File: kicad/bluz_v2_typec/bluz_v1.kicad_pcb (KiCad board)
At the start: 2 copper layers, 29.5 x 17.5 mm, 76 parts, among them J10 Conn, J11 Conn, J12 BTAnt, J2 Conn, J3 Conn, J4 Conn, J5 Conn, J6 Conn, J7 Conn, J8 Conn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

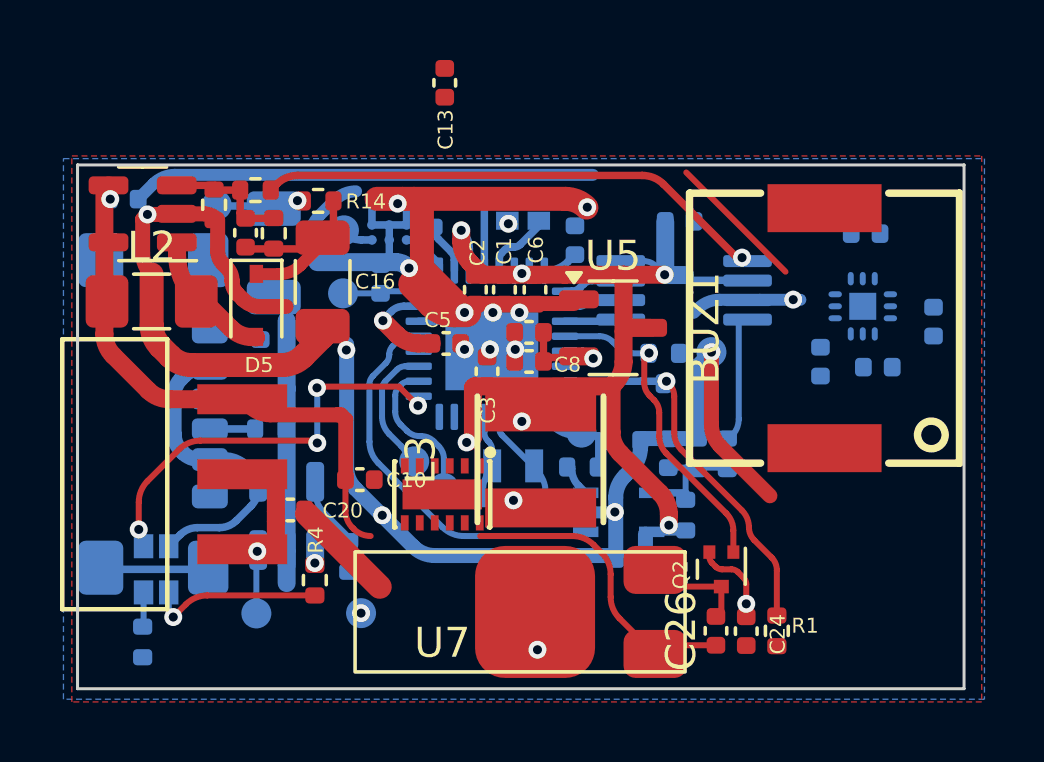
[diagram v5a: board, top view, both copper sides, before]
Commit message: удалено:       kicad/bluz_v2_typec/bluz_v1-backups/bluz_v1-2026-01-23_152519.zip 	изменено:      kicad/bluz_v2_typec/bluz_v1.kicad_pcb 	изменено:      kicad/bluz_v2_typec/bluz_v1.kicad_prl 	изменено:      kicad/bluz_v2_typec/bluz_v1.kicad_pro 	изменено:      kicad/bluz_v2_typec/bluz_v1.kicad_sch
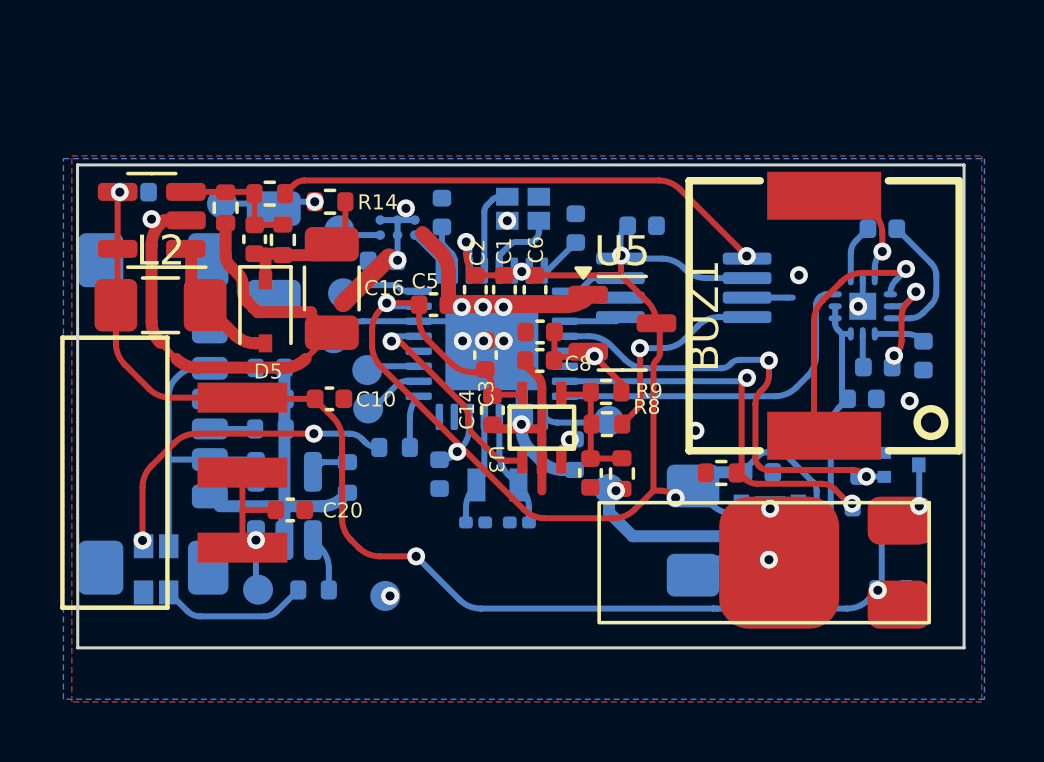
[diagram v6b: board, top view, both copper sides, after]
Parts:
- removed R7: 10k, Resistor_SMD:R_0402_1005Metric
- added C30: 22u, Capacitor_SMD:C_0402_1005Metric, B.Cu at (105.5, 55.8)
- C12, C14, R10, R2, R8, R9, U3: moved to F.Cu
- C13, C24, C26, Q2, R1, R4, U7: moved to B.Cu
- L3: footprint easyeda2kicad:IND-SMD_L4.0-W4.0_SMNR4018 -> Inductor_SMD:L_1206_3216Metric_Pad1.42x1.75mm_HandSolder; moved to B.Cu
- moved C13 16.7 mm to (116.1, 55.8), turned to 0 degrees
- moved U7 11.0 mm to (116.5, 57.9), turned to 90 degrees
- moved R5 10.6 mm to (104.0, 55.0), turned to 0 degrees
- moved M1 8.30 mm to (120.8, 58.8)
- moved C26 7.71 mm to (121.5, 57.4)
- moved R12 7.47 mm to (119.5, 55.4), turned to 90 degrees
- moved Q2 6.94 mm to (120.9, 55.5), turned to 0 degrees
- moved C14 6.75 mm to (107.3, 53.7), turned to -90 degrees
- moved J3 5.69 mm to (111.2, 56.3)
- moved L3 5.60 mm to (114.0, 57.7), turned to -90 degrees
- moved R1 5.13 mm to (119.8, 56.9), turned to 180 degrees
- moved C24 5.05 mm to (120.6, 59.7), turned to 180 degrees
- moved R9 4.89 mm to (111.0, 53.1), turned to 180 degrees
- moved R8 4.13 mm to (111.1, 54.2), turned to 180 degrees
- moved U3 3.81 mm to (108.9, 54.3), turned to 0 degrees
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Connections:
- C23 pad 1: /1.8v -> +1.8v
- C8 pad 1: /1.8v -> +1.8v
- D1 pad 5: /1.8v -> +1.8v
- LED1 pad 1: LED -> Net-(LED1-+-Pad1)
- LED1 pad 3: Net-(LED1---Pad3) -> GND
- R5 pad 1: Net-(LED1---Pad3) -> Net-(LED1-+-Pad1)
- R5 pad 2: GND -> LED
- R9 pad 1: +2V8 -> +1.8v
- U3 pad 3: Net-(U3-+) -> AIn
- U5 pad 2: /1.8v -> +1.8v
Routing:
- net GND: track 126.0 -> 67.6 mm, vias 21 -> 19
- net +BATT: track 30.0 -> 53.4 mm, vias 1 -> 3
- net +2V8: track 38.7 -> 54.7 mm
- net LED: track 13.8 -> 1.78 mm, vias 4 -> 0
- net Sound: track 0.00 -> 11.6 mm
- net Net-(LED1-+-Pad1): track 0.00 -> 10.7 mm, vias 0 -> 2
- net Net-(U6-VO1): track 0.00 -> 8.69 mm, vias 0 -> 1
- net Sync: track 13.1 -> 7.26 mm, vias 0 -> 1
- net Vibro: track 10.8 -> 15.5 mm, vias 1 -> 2
- net Net-(U6-CP1): track 0.00 -> 4.61 mm
- net +1.8v: track 0.00 -> 4.58 mm, vias 0 -> 1
- net /1.8v: track 3.44 -> 0.00 mm, vias 1 -> 0
- net Net-(U6-CN2): track 0.00 -> 3.34 mm, vias 0 -> 2
- net /swd: track 4.72 -> 1.86 mm
- net /swc: track 5.00 -> 2.18 mm
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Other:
- board size 29.5 x 17.5 mm -> 29.6 x 16.1 mm

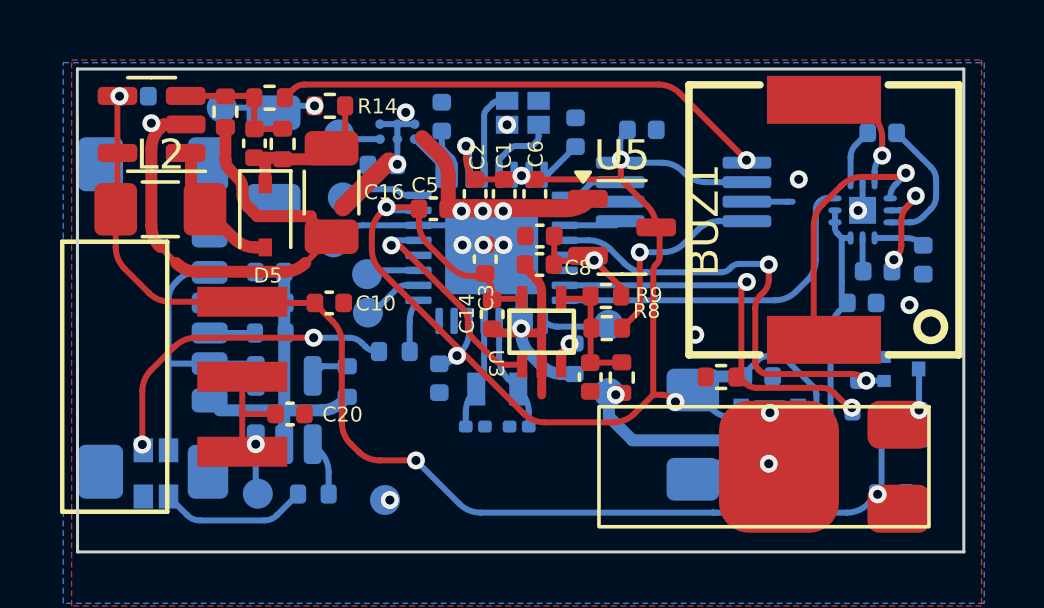
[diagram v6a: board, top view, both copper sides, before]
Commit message: удалено:       kicad/bluz_v2_typec/bluz_v1-backups/bluz_v1-2026-01-27_180557.zip 	удалено:       kicad/bluz_v2_typec/bluz_v1-backups/bluz_v1-2026-01-27_191409.zip 	удалено:       kicad/bluz_v2_typec/bluz_v1-backups/bluz_v1-2026-01-28_075426.zip 	удалено:       kicad/bluz_v2_typec/bluz_v1-backups/bluz_v1-2026-02-14_111146.zip 	удалено:       kicad/bluz_v2_typec/bluz_v1-backups/bluz_v1-2026-02-14_111739.zip 	изменено:      kicad/bluz_v2_typec/bluz_v1.kicad_pcb 	изменено:      kicad/bluz_v2_typec/bluz_v1.kicad_prl
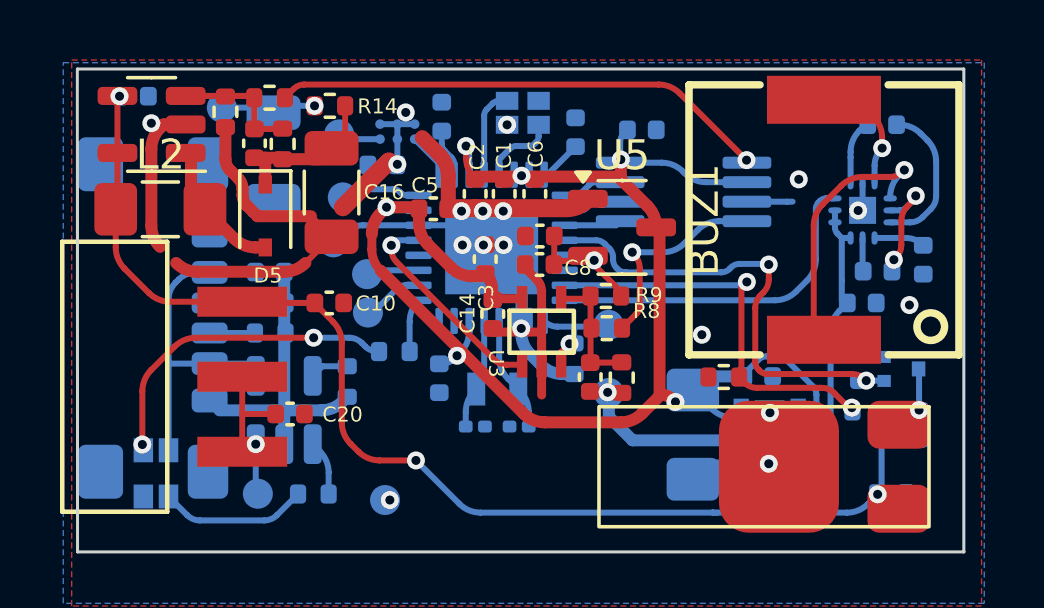
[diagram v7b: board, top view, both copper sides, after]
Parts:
- moved C28 0.27 mm to (120.3, 47.4)
- moved R2 0.09 mm to (115.0, 55.8)
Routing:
- net GND: track 67.6 -> 66.8 mm
- net cmpAdj: track 6.45 -> 6.98 mm
- net Net-(U6-CP1): track 4.61 -> 5.11 mm

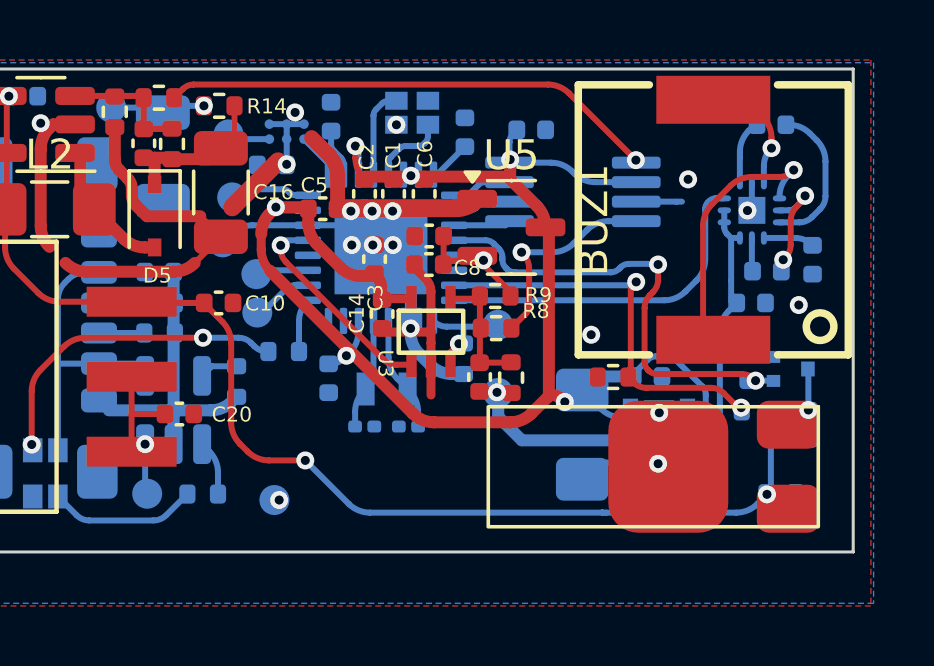
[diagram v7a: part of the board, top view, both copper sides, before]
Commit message: удалено:       kicad/bluz_v2_typec/bluz_v1-backups/bluz_v1-2026-02-14_112253.zip 	удалено:       kicad/bluz_v2_typec/bluz_v1-backups/bluz_v1-2026-02-14_192355.zip 	изменено:      kicad/bluz_v2_typec/bluz_v1.kicad_pcb 	изменено:      kicad/bluz_v2_typec/fp-info-cache 	изменено:      stm32cubeide/BluZ_LPM/BluZ_LPM_v1.ioc 	изменено:      stm32cubeide/BluZ_LPM/Core/Src/main.c 	изменено:      stm32cubeide/BluZ_LPM/Release/BluZ_LPM_v1.elf
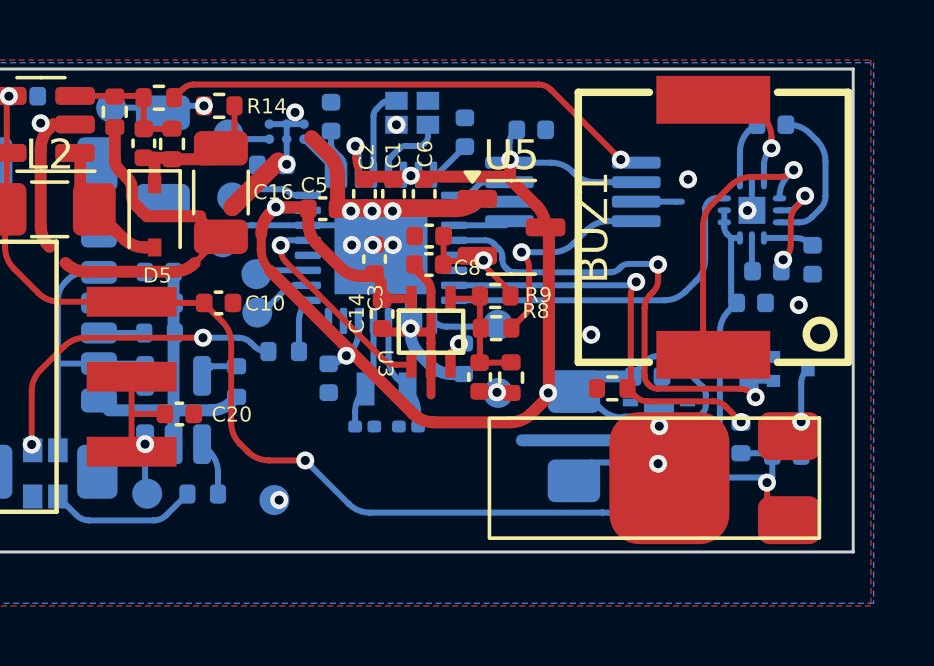
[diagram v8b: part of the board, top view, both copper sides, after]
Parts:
- moved C24 1.28 mm to (120.8, 58.4)
- moved R1 1.05 mm to (119.2, 57.8), turned to 90 degrees
- moved C26 0.72 mm to (120.8, 57.4), turned to 0 degrees
- moved M1 0.38 mm to (120.9, 59.2)
- moved R2 0.38 mm to (115.0, 56.2)
- moved L3 0.28 mm to (113.7, 57.8)
- moved BUZ1 0.25 mm to (118.3, 50.8)
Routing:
- net GND: track 66.8 -> 64.9 mm
- net +BATT: track 53.4 -> 52.2 mm
- net Vibro: track 15.8 -> 16.9 mm
- net +2V8: track 54.7 -> 54.2 mm
- net batLev: track 13.3 -> 13.8 mm
